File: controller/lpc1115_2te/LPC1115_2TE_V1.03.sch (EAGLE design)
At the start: 57 parts, among them IC1 LPC1115, IC2 BD9G101, Q1 BC856, Q2 BC847C, Q3 BCP52, Q4 ASFL

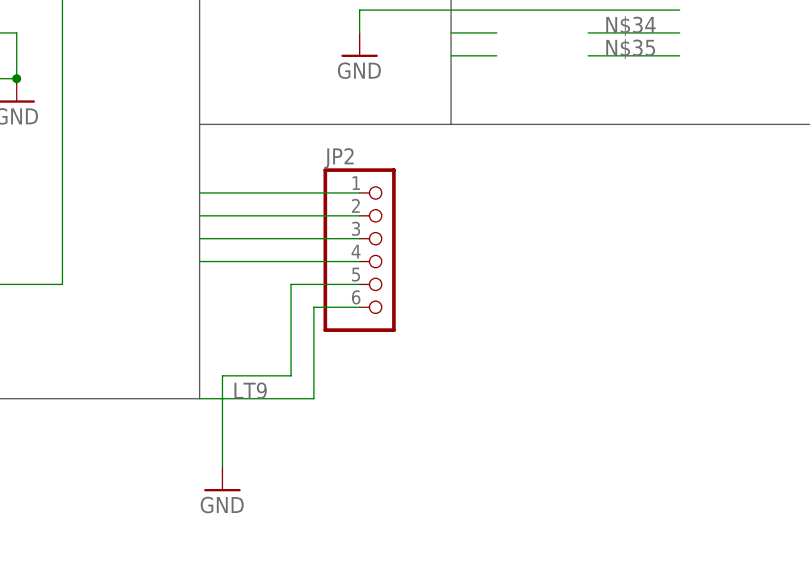
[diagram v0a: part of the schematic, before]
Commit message: LPC1115 2TE V3 zusätzlicher VCC PIN zur LED Platine
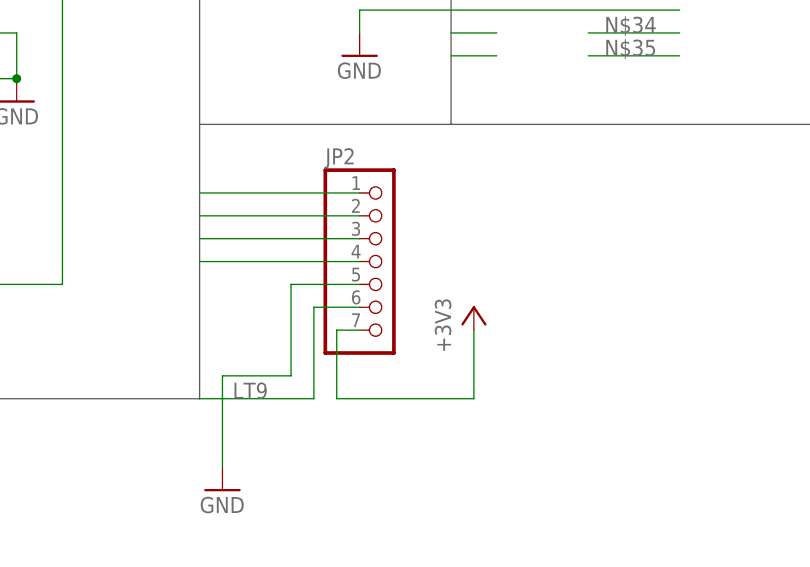
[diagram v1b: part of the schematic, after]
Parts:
- JP2: device pinhead:PINHD-1X6 -> pinhead:PINHD-1X7
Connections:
- net VCC: now also JP2.7
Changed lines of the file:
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@@
 <part name="L2" library="inductor-neosid" deviceset="BS" device="11" value="150mH"/>
 <part name="JP1" library="pinhead" deviceset="PINHD-1X9" device=""/>
-<part name="JP2" library="pinhead" deviceset="PINHD-1X6" device=""/>
 <part name="R12" library="rcl" deviceset="R-EU_" device="R1206" value="10k"/>
 <part name="FRAME1" library="frames" deviceset="DINA4_L" device=""/>
@@
 <part name="C11" library="rcl" deviceset="C-EU" device="C1206" value="10n"/>
 <part name="Q4" library="crystal" deviceset="ASF*" device="" technology="L"/>
+<part name="JP2" library="pinhead" deviceset="PINHD-1X7" device=""/>
+<part name="P+11" library="supply1" deviceset="+3V3" device=""/>
 </parts>
 <sheets>
@@
 <instance part="L2" gate="G$1" x="73.66" y="119.38"/>
 <instance part="JP1" gate="A" x="22.86" y="73.66" rot="MR0"/>
-<instance part="JP2" gate="A" x="342.9" y="91.44"/>
 <instance part="R12" gate="G$1" x="104.14" y="99.06"/>
 <instance part="FRAME1" gate="G$2" x="162.56" y="0"/>
@@
 <instance part="C11" gate="G$1" x="172.72" y="68.58" rot="R180"/>
 <instance part="Q4" gate="G$1" x="190.5" y="71.12"/>
+<instance part="JP2" gate="A" x="342.9" y="91.44"/>
+<instance part="P+11" gate="G$1" x="353.06" y="86.36"/>
 </instances>
 <busses>
@@
 <pinref part="GND16" gate="1" pin="GND"/>
 <wire x1="332.74" y1="78.74" x2="332.74" y2="88.9" width="0.1524" layer="91"/>
+<wire x1="332.74" y1="88.9" x2="340.36" y2="88.9" width="0.1524" layer="91"/>
 <pinref part="JP2" gate="A" pin="5"/>
-<wire x1="332.74" y1="88.9" x2="340.36" y2="88.9" width="0.1524" layer="91"/>
 </segment>
 <segment>
@@
 <pinref part="Q4" gate="G$1" pin="OE"/>
 </segment>
+<segment>
+<pinref part="JP2" gate="A" pin="7"/>
+<wire x1="340.36" y1="83.82" x2="337.82" y2="83.82" width="0.1524" layer="91"/>
+<wire x1="337.82" y1="83.82" x2="337.82" y2="76.2" width="0.1524" layer="91"/>
+<wire x1="337.82" y1="76.2" x2="353.06" y2="76.2" width="0.1524" layer="91"/>
+<pinref part="P+11" gate="G$1" pin="+3V3"/>
+<wire x1="353.06" y1="76.2" x2="353.06" y2="83.82" width="0.1524" layer="91"/>
+</segment>
 </net>
 <net name="PWM" class="0">
@@
 </segment>
 <segment>
+<wire x1="322.58" y1="99.06" x2="340.36" y2="99.06" width="0.1524" layer="91"/>
 <pinref part="JP2" gate="A" pin="1"/>
-<wire x1="322.58" y1="99.06" x2="340.36" y2="99.06" width="0.1524" layer="91"/>
 </segment>
 </net>
@@
 </segment>
 <segment>
+<wire x1="322.58" y1="91.44" x2="340.36" y2="91.44" width="0.1524" layer="91"/>
 <pinref part="JP2" gate="A" pin="4"/>
-<wire x1="322.58" y1="91.44" x2="340.36" y2="91.44" width="0.1524" layer="91"/>
 </segment>
 </net>
@@
 </segment>
 <segment>
+<wire x1="322.58" y1="96.52" x2="340.36" y2="96.52" width="0.1524" layer="91"/>
 <pinref part="JP2" gate="A" pin="2"/>
-<wire x1="322.58" y1="96.52" x2="340.36" y2="96.52" width="0.1524" layer="91"/>
 </segment>
 </net>
@@
 <wire x1="322.58" y1="76.2" x2="335.28" y2="76.2" width="0.1524" layer="91"/>
 <wire x1="335.28" y1="76.2" x2="335.28" y2="86.36" width="0.1524" layer="91"/>
+<wire x1="335.28" y1="86.36" x2="340.36" y2="86.36" width="0.1524" layer="91"/>
 <pinref part="JP2" gate="A" pin="6"/>
-<wire x1="335.28" y1="86.36" x2="340.36" y2="86.36" width="0.1524" layer="91"/>
 </segment>
 <segment>
@@
 </segment>
 <segment>
+<wire x1="322.58" y1="93.98" x2="340.36" y2="93.98" width="0.1524" layer="91"/>
 <pinref part="JP2" gate="A" pin="3"/>
-<wire x1="322.58" y1="93.98" x2="340.36" y2="93.98" width="0.1524" layer="91"/>
-</segment>
-</net>
+</segment>
+</net>
